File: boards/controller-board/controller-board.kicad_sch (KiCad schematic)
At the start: 67 parts, among them J1 Conn_01x02, J2 Conn_01x02, J3 Conn_01x02, J4 Conn_01x02, J5 Conn_01x03, J6 Phoenix 1995499, Q1 PMV45EN, Q2 Goford_G11S_20V_11A, SW1 EG1271, U1 LTC3624, U2 ADS1015IRUGR, U3 ADS1015IRUGR, U4 RPi_Pico, U5 MCP4728

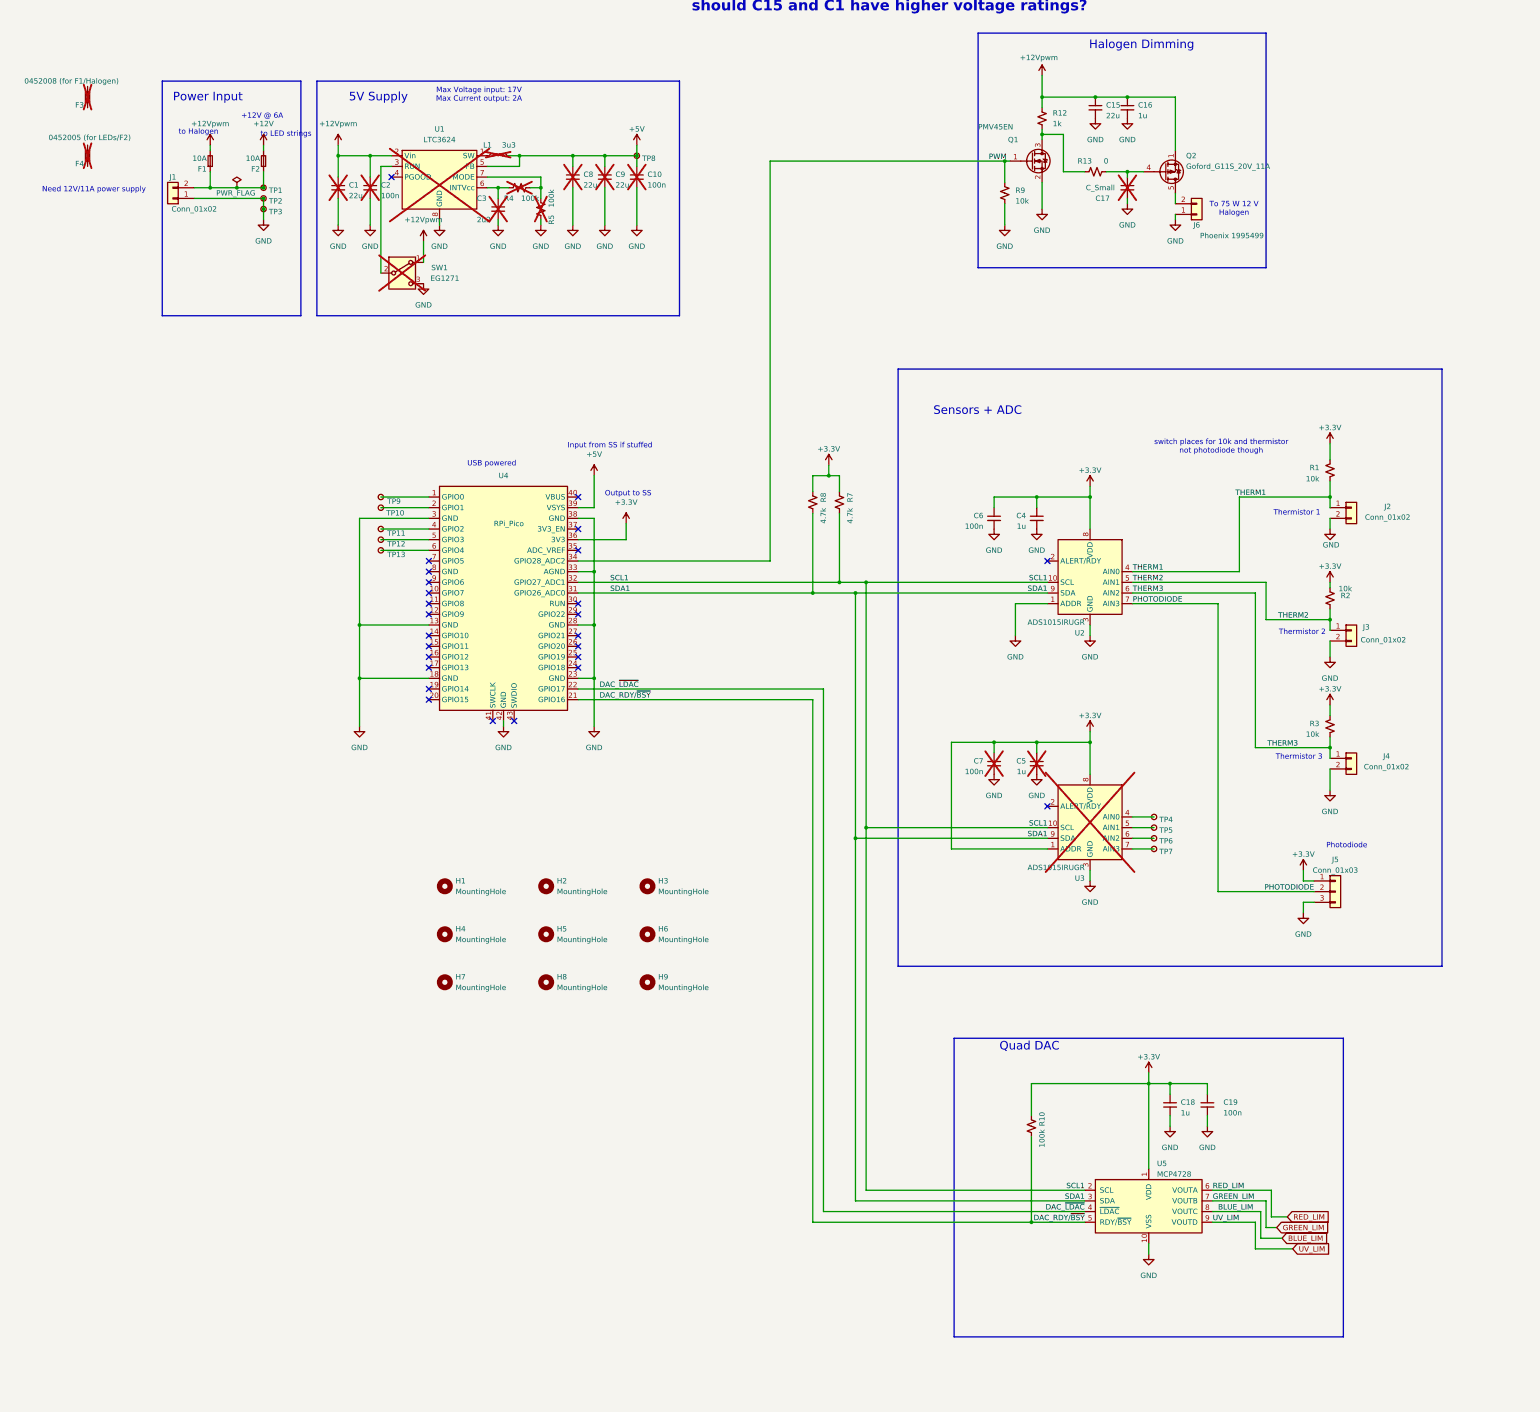
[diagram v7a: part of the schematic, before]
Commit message: removed 100k pull-down resistors from LED drivers and added a 100k resistor to each output of DAC, other misc schematic and pcb changes
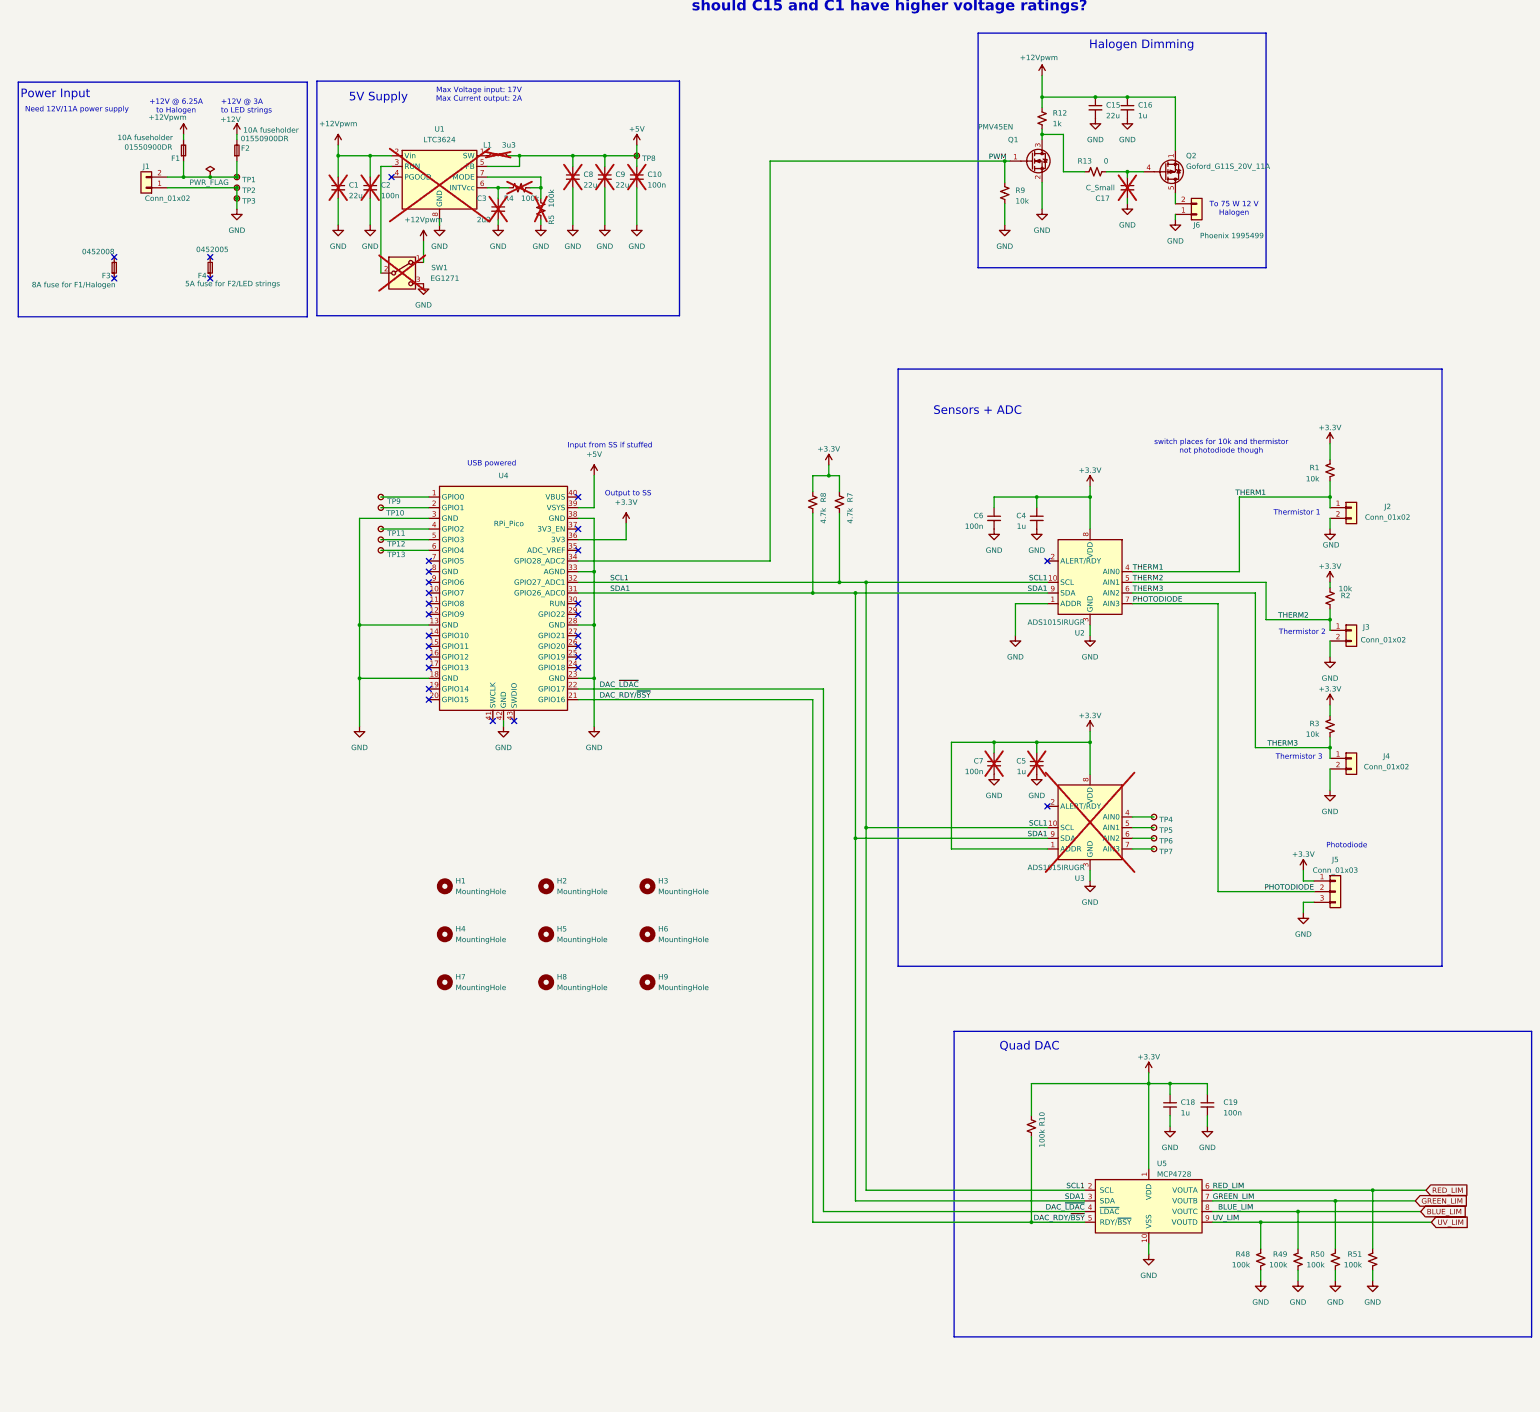
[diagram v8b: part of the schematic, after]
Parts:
- added R48, R49, R50, R51: 100k, oresat-passives:0603-C, symbol Device:R_Small_US
- F1, F2: value 10A -> 01550900DR
- F3: value 0452008 (for F1/Halogen) -> 0452008; now fitted
- F4: value 0452005 (for LEDs/F2) -> 0452005; now fitted
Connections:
- net BLUE_LIM: now also R49.1
- net GND: now also R48.2, R49.2, R50.2, R51.2
- net GREEN_LIM: now also R50.1
- net RED_LIM: now also R51.1
- net UV_LIM: now also R48.1
- no-connect marks 26 -> 30
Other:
- note added: "+12V @ 3A to LED strings"
- note added: "+12V @ 6.25A to Halogen"
- note removed: "+12V @ 6A"
- note removed: "to Halogen"
- note removed: "to LED strings"
- moved on the sheet: F1, F2, J1, TP1, TP2, TP3
